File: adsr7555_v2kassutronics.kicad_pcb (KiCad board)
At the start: 2 copper layers, 78.7 x 106.7 mm, 43 parts, among them J1 Power, J2 GateIn, J5 InvOut, J6 Output, Q1 3904, Q2 3904, Q3 3904, SW1 SW_Trig, U1 7555, U2 TL074

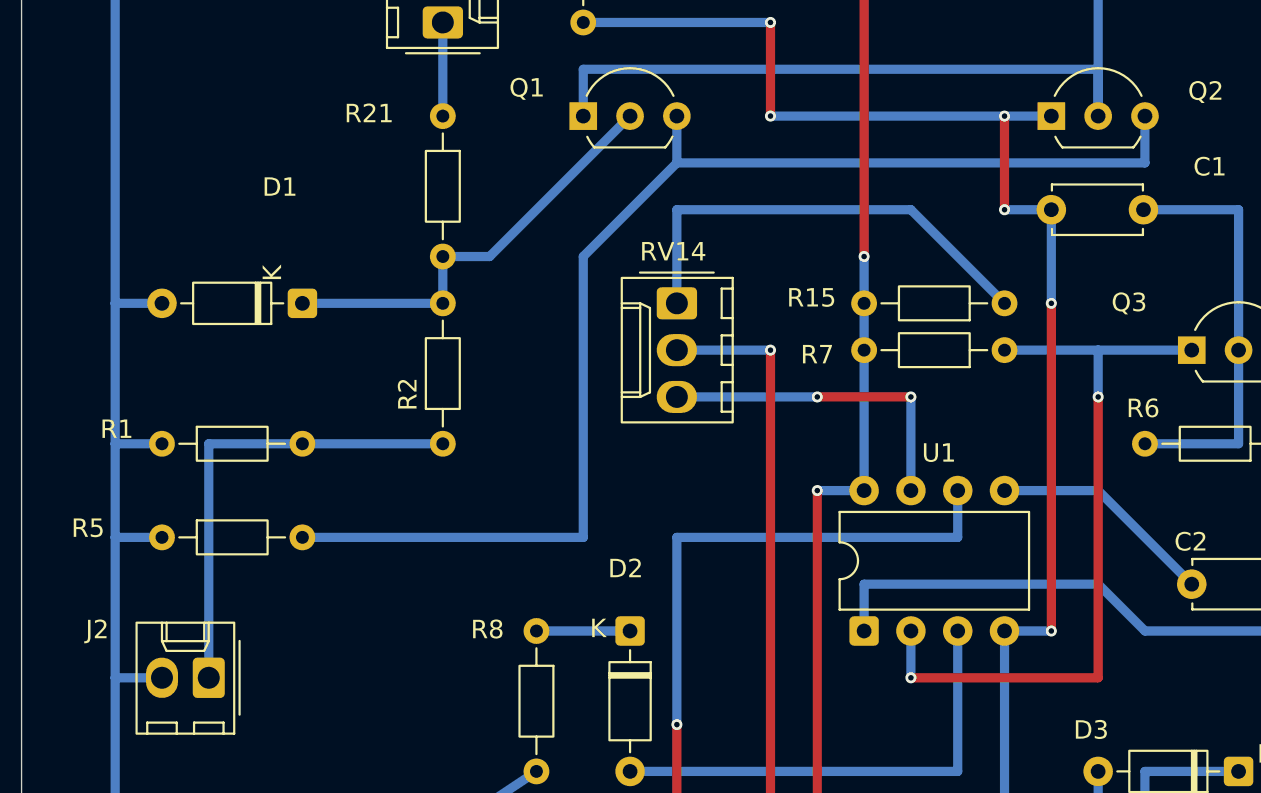
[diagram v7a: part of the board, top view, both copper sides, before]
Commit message: top 1/3 pCB wired
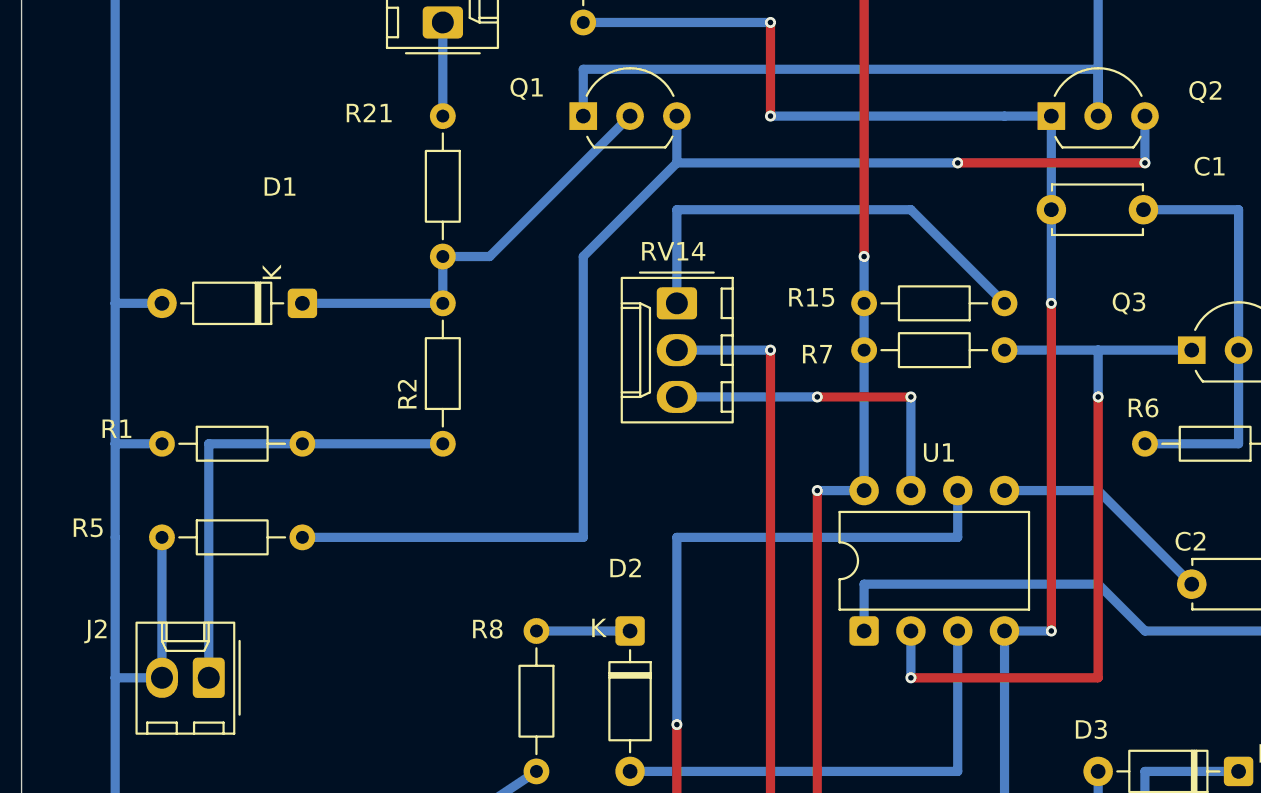
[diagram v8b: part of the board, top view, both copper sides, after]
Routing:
- net GND: track 331.8 -> 336.9 mm
- net GATE: track 84.9 -> 82.3 mm, vias 6 -> 4
- net Net-(Q1-E): vias 0 -> 2
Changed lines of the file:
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@@
+	)
+	(segment
+		(start 101.6 58.42)
+		(end 91.44 58.42)
+		(width 0.5)
+		(layer "F.Cu")
+		(net "Net-(Q1-E)")
+	)
+	(via
+		(at 101.6 58.42)
+		(size 0.6)
+		(drill 0.3)
+		(layers "F.Cu" "B.Cu")
+		(net "Net-(Q1-E)")
+	)
+	(via
+		(at 91.44 58.42)
+		(size 0.6)
+		(drill 0.3)
+		(layers "F.Cu" "B.Cu")
+		(net "Net-(Q1-E)")
 	)
 	(segment
@@
 	)
 	(segment
-		(start 76.2 58.42)
-		(end 101.6 58.42)
+		(start 91.44 58.42)
+		(end 76.2 58.42)
 		(width 0.5)
 		(layer "B.Cu")
@@
 	)
 	(segment
-		(start 48.26 78.74)
-		(end 45.72 78.74)
-		(width 0.5)
-		(layer "B.Cu")
-		(net "GND")
-	)
-	(segment
 		(start 109.22 83.82)
 		(end 101.6 83.82)
@@
 	)
 	(segment
+		(start 48.26 78.74)
+		(end 48.26 86.36)
+		(width 0.5)
+		(layer "B.Cu")
+		(net "GND")
+	)
+	(segment
 		(start 81.28 33.02)
 		(end 81.28 30.48)
@@
 	)
 	(segment
-		(start 93.98 60.96)
-		(end 93.98 55.88)
-		(width 0.5)
-		(layer "F.Cu")
-		(net "GATE")
-	)
-	(segment
 		(start 81.28 50.8)
 		(end 81.28 55.88)
@@
 	)
 	(via
-		(at 93.98 55.88)
-		(size 0.6)
-		(drill 0.3)
-		(layers "F.Cu" "B.Cu")
-		(net "GATE")
-	)
-	(via
 		(at 96.52 83.82)
 		(size 0.6)
@@
 	(via
 		(at 81.28 55.88)
-		(size 0.6)
-		(drill 0.3)
-		(layers "F.Cu" "B.Cu")
-		(net "GATE")
-	)
-	(via
-		(at 93.98 60.96)
 		(size 0.6)
 		(drill 0.3)
@@
 	)
 	(segment
+		(start 96.52 55.88)
+		(end 96.52 60.96)
+		(width 0.5)
+		(layer "B.Cu")
+		(net "GATE")
+	)
+	(segment
 		(start 96.52 83.82)
 		(end 93.98 83.82)
@@
 		(width 0.5)
 		(layer "B.Cu")
-		(net "GATE")
-	)
-	(segment
-		(start 96.52 60.96)
-		(end 93.98 60.96)
-		(width 0.5)
-		(layer "B.Cu")
